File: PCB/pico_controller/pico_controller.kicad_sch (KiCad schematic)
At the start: 22 parts, among them J1 Conn_01x04, J10 Conn_01x03, J11 Conn_01x03, J2 Conn_01x04, J3 Conn_01x04, J4 Conn_01x12, J5 Conn_01x04, J6 Conn_01x02, J7 Conn_01x02, J8 Conn_01x04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

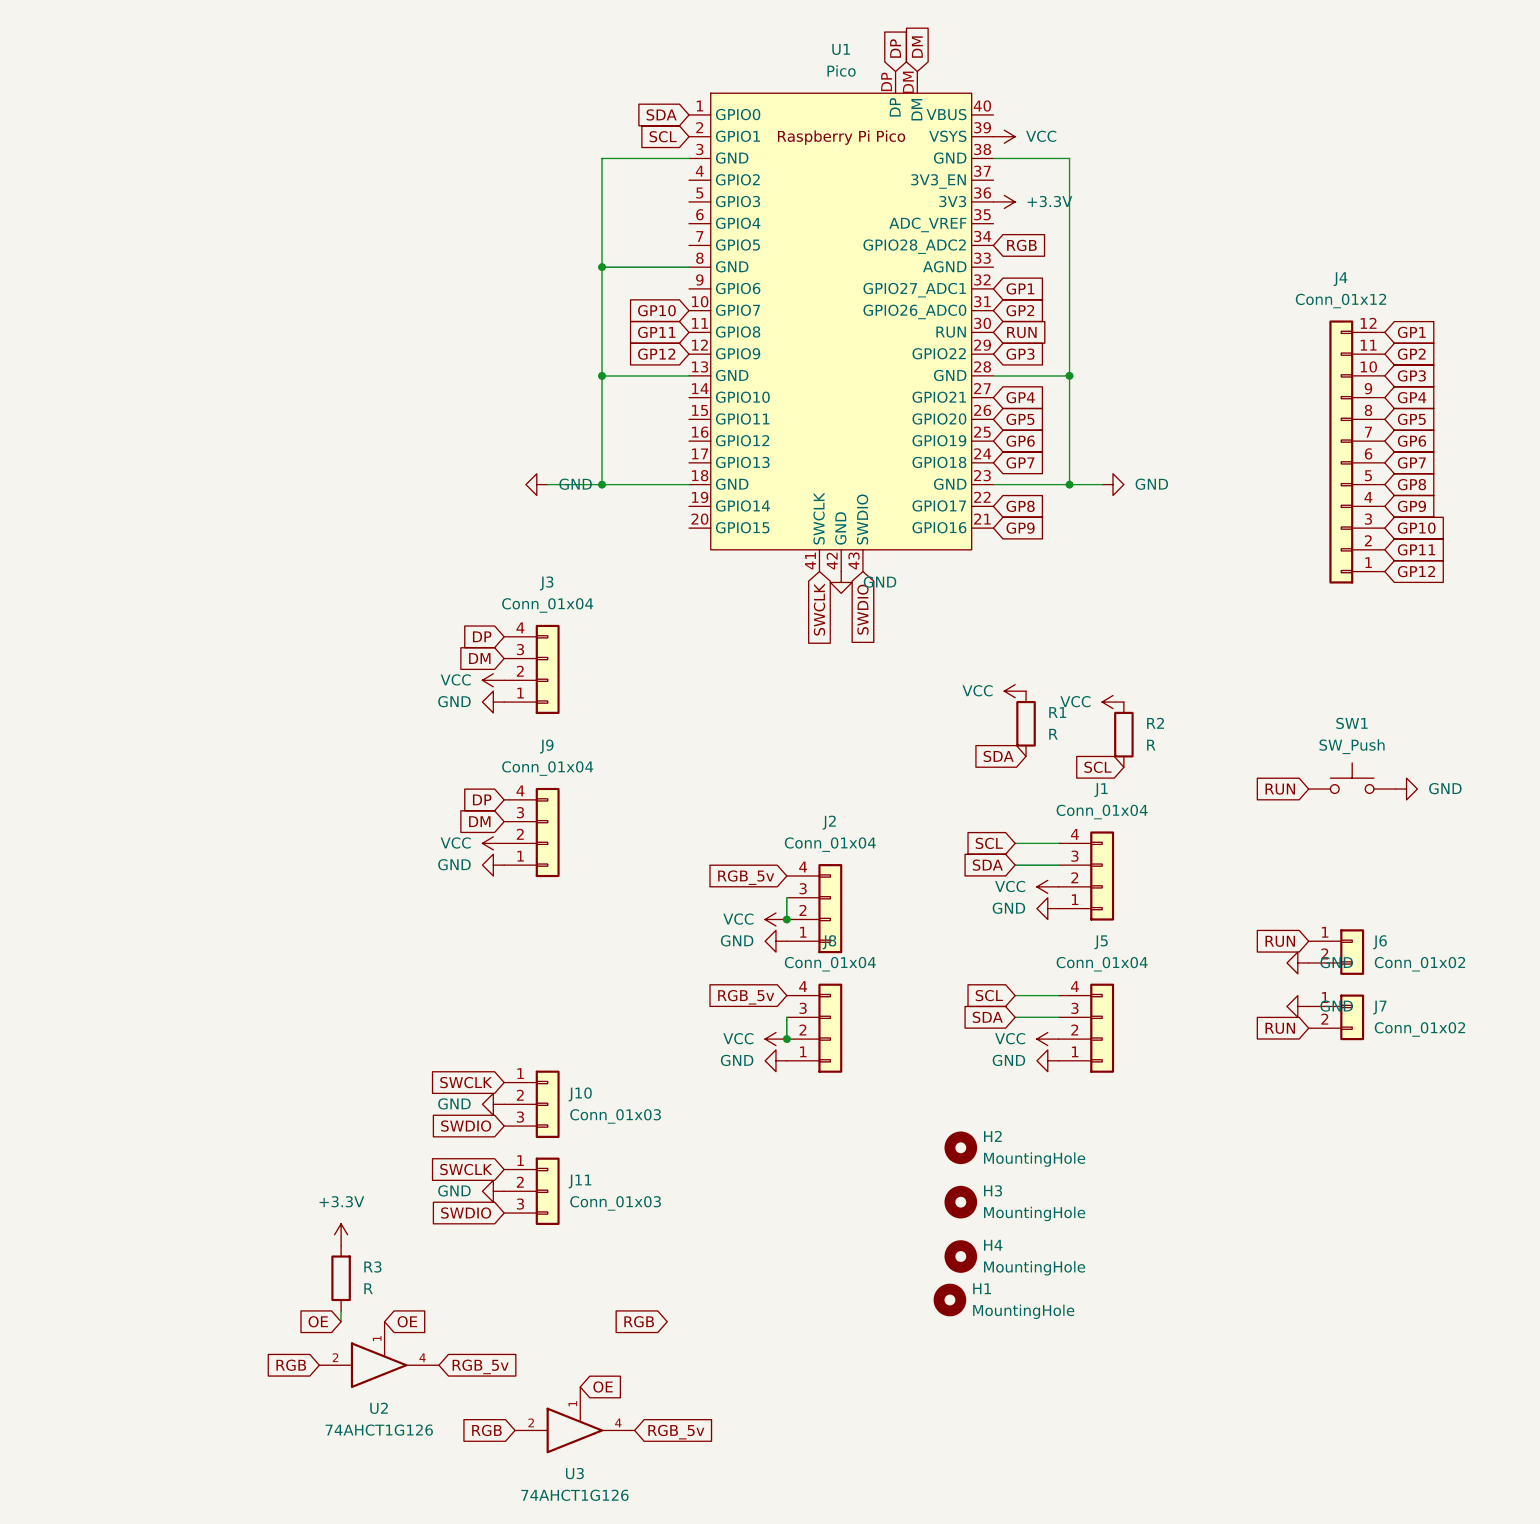
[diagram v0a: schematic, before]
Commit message: add handness jumper to controller
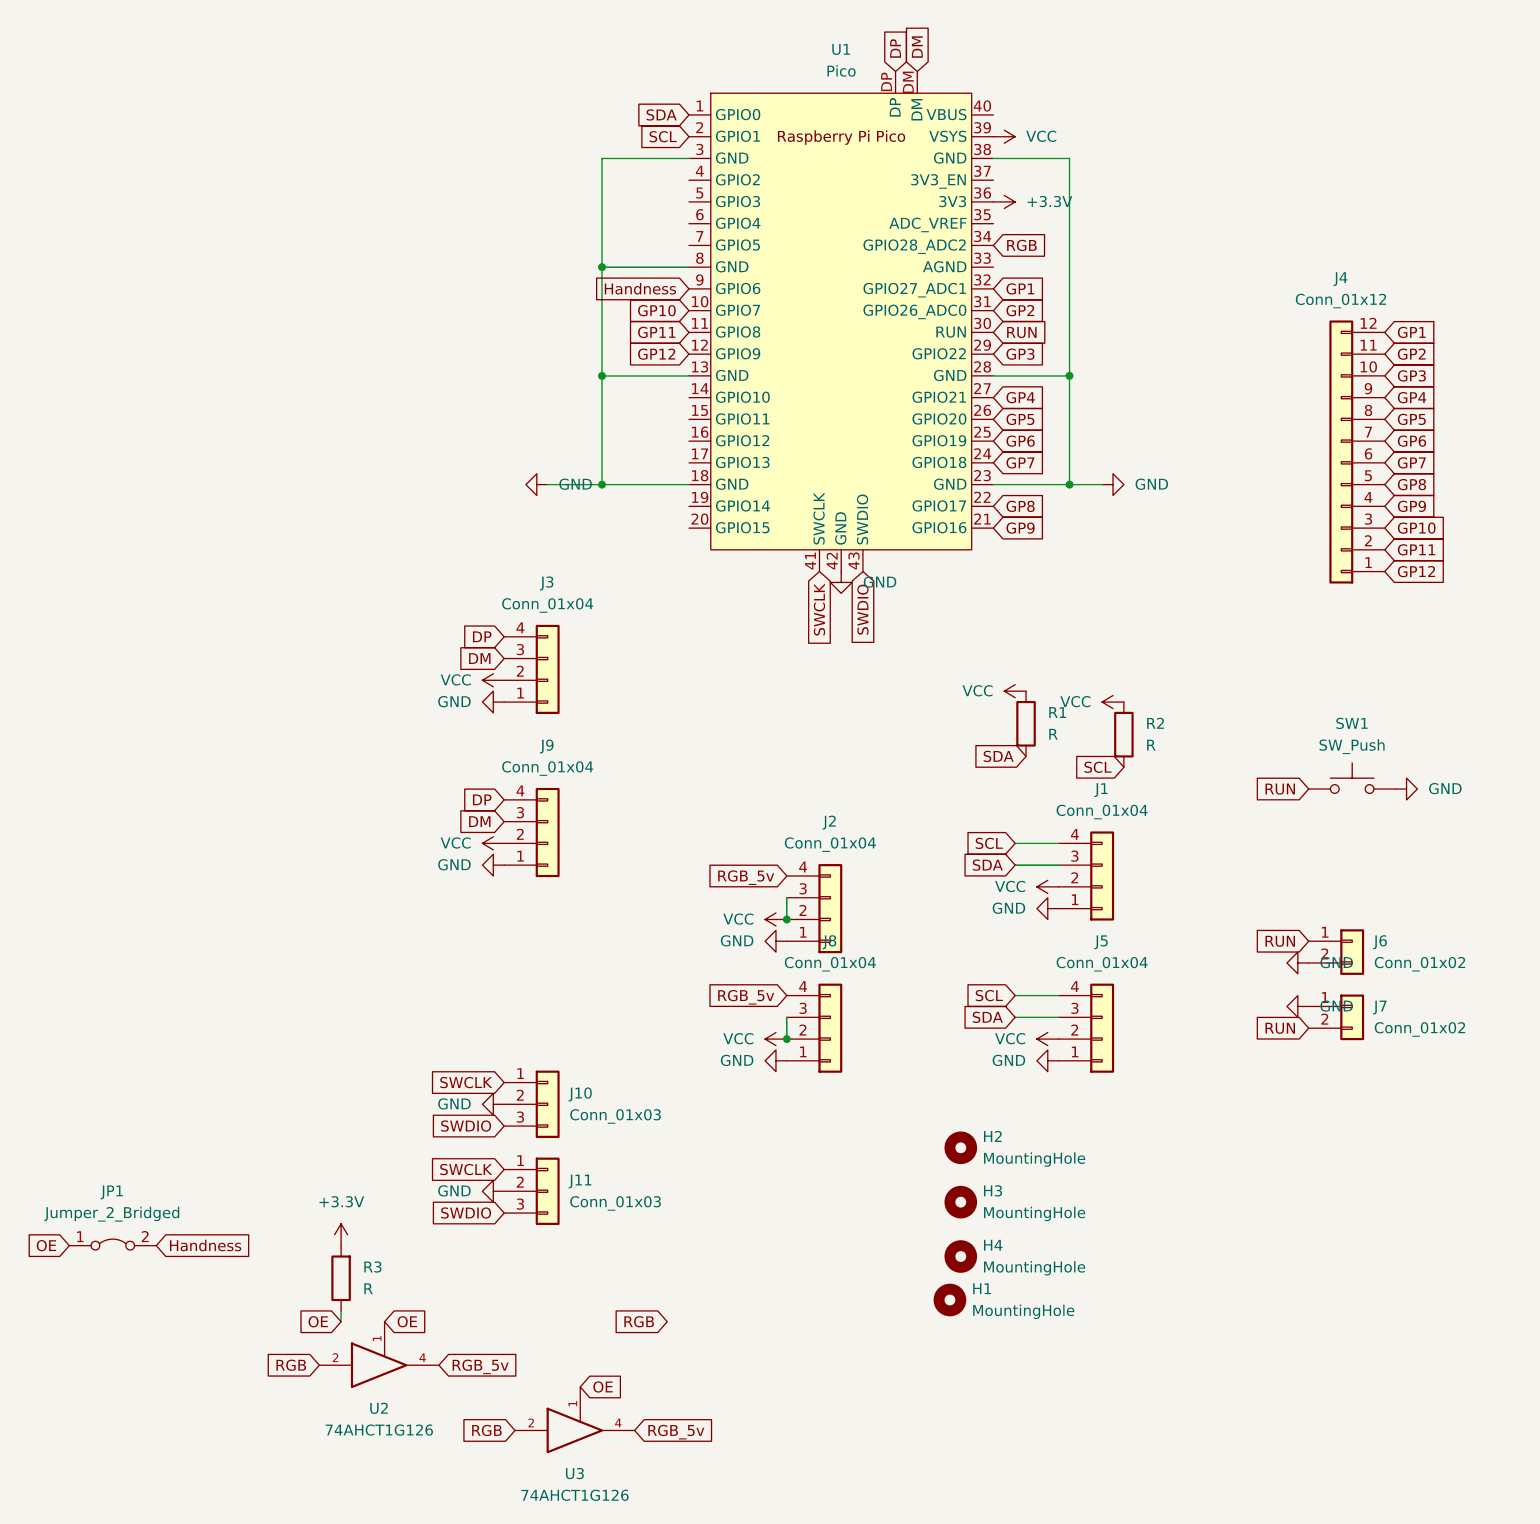
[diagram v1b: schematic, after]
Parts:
- added JP1: Jumper_2_Bridged, Jumper:SolderJumper-2_P1.3mm_Open_RoundedPad1.0x1.5mm, symbol Jumper:Jumper_2_Bridged
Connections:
- net OE: now also JP1.1 (A)
- net Handness: now reaches U1.9 (GPIO6)
- net Handness: now also JP1.2 (B)
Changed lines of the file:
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@@
+    )
+  )
+  (global_label "OE" (shape input) (at 44.45 166.37 180) (fields_autoplaced)
+    (effects (font (size 1.27 1.27)) (justify right))
+    (property "Intersheet References" "${INTERSHEET_REFS}" (id 0) (at 39.5574 166.2906 0)
+      (effects (font (size 1.27 1.27)) (justify right) hide)
     )
   )
@@
     )
   )
+  (global_label "Handness" (shape input) (at 116.84 54.61 180) (fields_autoplaced)
+    (effects (font (size 1.27 1.27)) (justify right))
+    (property "Intersheet References" "${INTERSHEET_REFS}" (id 0) (at 105.3555 54.6894 0)
+      (effects (font (size 1.27 1.27)) (justify right) hide)
+    )
+  )
   (global_label "DM" (shape input) (at 95.25 116.84 180) (fields_autoplaced)
     (effects (font (size 1.27 1.27)) (justify right))
@@
     (property "Intersheet References" "${INTERSHEET_REFS}" (id 0) (at 110.9193 36.7506 0)
       (effects (font (size 1.27 1.27)) (justify right) hide)
+    )
+  )
+  (global_label "Handness" (shape input) (at 54.61 166.37 0) (fields_autoplaced)
+    (effects (font (size 1.27 1.27)) (justify left))
+    (property "Intersheet References" "${INTERSHEET_REFS}" (id 0) (at 66.0945 166.2906 0)
+      (effects (font (size 1.27 1.27)) (justify left) hide)
     )
   )
@@
     (pin "2")
   )
+  (symbol (lib_id "Jumper:Jumper_2_Bridged") (at 49.53 166.37 0) (unit 1)
+    (in_bom yes) (on_board yes) (fields_autoplaced)
+    (property "Reference" "JP1" (id 0) (at 49.53 160.02 0))
+    (property "Value" "Jumper_2_Bridged" (id 1) (at 49.53 162.56 0))
+    (property "Footprint" "Jumper:SolderJumper-2_P1.3mm_Open_RoundedPad1.0x1.5mm" (id 2) (at 49.53 166.37 0)
+      (effects (font (size 1.27 1.27)) hide)
+    )
+    (property "Datasheet" "~" (id 3) (at 49.53 166.37 0)
+      (effects (font (size 1.27 1.27)) hide)
+    )
+    (pin "1")
+    (pin "2")
+  )
   (symbol (lib_id "Mechanical:MountingHole") (at 148.59 154.94 0) (unit 1)
     (in_bom yes) (on_board yes) (fields_autoplaced)
@@
       (reference "J11") (unit 1) (value "Conn_01x03") (footprint "Connector_JST:JST_SH_SM03B-SRSS-TB_1x03-1MP_P1.00mm_Horizontal")
     )
+    (path "/a148a7a0-32ef-4104-ad3e-fced193791c4"
+      (reference "JP1") (unit 1) (value "Jumper_2_Bridged") (footprint "Jumper:SolderJumper-2_P1.3mm_Open_RoundedPad1.0x1.5mm")
+    )
     (path "/88a7e450-fad7-4922-8293-5907d9a65aab"

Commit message: firmware init
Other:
- note added: "GPIO07"
- note added: "GPIO08"
- note added: "GPIO09"
- note added: "GPIO16"
- note added: "GPIO17"
- note added: "GPIO18"
- note added: "GPIO19"
- note added: "GPIO20"
- note added: "GPIO21"
- note added: "GPIO22"
- note added: "GPIO26"
- note added: "GPIO27"
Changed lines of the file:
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@@
     (stroke (width 0) (type default) (color 0 0 0 0))
+  )
+  (text "GPIO27" (at 204.47 60.96 0)
+    (effects (font (size 1.27 1.27)) (justify left bottom))
+  )
+  (text "GPIO08" (at 205.74 86.36 0)
+    (effects (font (size 1.27 1.27)) (justify left bottom))
+  )
+  (text "GPIO22" (at 204.47 66.04 0)
+    (effects (font (size 1.27 1.27)) (justify left bottom))
+  )
+  (text "GPIO18" (at 204.47 76.2 0)
+    (effects (font (size 1.27 1.27)) (justify left bottom))
+  )
+  (text "GPIO21" (at 204.47 68.58 0)
+    (effects (font (size 1.27 1.27)) (justify left bottom))
+  )
+  (text "GPIO20" (at 204.47 71.12 0)
+    (effects (font (size 1.27 1.27)) (justify left bottom))
+  )
+  (text "GPIO17" (at 204.47 78.74 0)
+    (effects (font (size 1.27 1.27)) (justify left bottom))
+  )
+  (text "GPIO16" (at 204.47 81.28 0)
+    (effects (font (size 1.27 1.27)) (justify left bottom))
+  )
+  (text "GPIO26\n" (at 204.47 63.5 0)
+    (effects (font (size 1.27 1.27)) (justify left bottom))
+  )
+  (text "GPIO19" (at 204.47 73.66 0)
+    (effects (font (size 1.27 1.27)) (justify left bottom))
+  )
+  (text "GPIO07" (at 205.74 83.82 0)
+    (effects (font (size 1.27 1.27)) (justify left bottom))
+  )
+  (text "GPIO09" (at 205.74 88.9 0)
+    (effects (font (size 1.27 1.27)) (justify left bottom))
   )
   (global_label "DP" (shape input) (at 95.25 114.3 180) (fields_autoplaced)
